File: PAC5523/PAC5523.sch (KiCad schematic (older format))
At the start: 122 parts, among them J1 CON_HALL, J2 U, J3 V, J4 W, J5 UART, J6 SWD, J7 CAN, J8 NTC, Q1 Q_NMOS_GDS, T1 Transformer_1P_1S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

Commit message: updated connectors
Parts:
- removed J1: CON_HALL, Connector_Molex:Molex_PicoBlade_53261-0571_1x05-1MP_P1.25mm_Horizontal, symbol Connector:Conn_01x06_Male
- removed J5: UART, Connector_Molex:Molex_PicoBlade_53261-0471_1x04-1MP_P1.25mm_Horizontal, symbol Connector:Conn_01x05_Male
- removed J7: CAN, Connector_Molex:Molex_PicoBlade_53261-0371_1x03-1MP_P1.25mm_Horizontal, symbol Connector:Conn_01x04_Male
- removed J8: NTC, Connector_Molex:Molex_PicoBlade_53261-0271_1x02-1MP_P1.25mm_Horizontal, symbol Connector:Conn_01x03_Male
- removed J?: LED, Connector_Molex:Molex_PicoBlade_53261-0371_1x03-1MP_P1.25mm_Horizontal, symbol Connector:Conn_01x04_Male
- added J1: UART, Connector_Molex:Molex_PicoBlade_53261-0471_1x04-1MP_P1.25mm_Horizontal, symbol Connector_Generic_MountingPin:Conn_01x04_MountingPin
- added J5: HALL, Connector_Molex:Molex_PicoBlade_53261-0571_1x05-1MP_P1.25mm_Horizontal, symbol Connector_Generic_MountingPin:Conn_01x05_MountingPin
- added J7: CAN, Connector_Molex:Molex_PicoBlade_53261-0371_1x03-1MP_P1.25mm_Horizontal, symbol Connector_Generic_MountingPin:Conn_01x03_MountingPin
- added J8: NTC, Connector_Molex:Molex_PicoBlade_53261-0271_1x02-1MP_P1.25mm_Horizontal, symbol Connector_Generic_MountingPin:Conn_01x02_MountingPin
- added J9: LED, Connector_Molex:Molex_PicoBlade_53261-0371_1x03-1MP_P1.25mm_Horizontal, symbol Connector_Generic_MountingPin:Conn_01x03_MountingPin
- gave numbers to parts that had none: 1
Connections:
- wire segments 190 -> 187
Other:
- moved on the sheet: R40
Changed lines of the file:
@@
 Text GLabel 2200 3800 3    50   Input ~ 0
 SK6812
-$Comp
-L Connector:Conn_01x04_Male J?
-U 1 1 5D45B5D1
-P 9200 9050
-F 0 "J?" H 9172 8932 50  0000 R CNN
-F 1 "LED" H 9172 9023 50  0000 R CNN
-F 2 "Connector_Molex:Molex_PicoBlade_53261-0371_1x03-1MP_P1.25mm_Horizontal" H 9200 9050 50  0001 C CNN
-F 3 "~" H 9200 9050 50  0001 C CNN
-	1    9200 9050
-	-1   0    0    1
-$EndComp
 Text GLabel 9000 9050 0    50   Input ~ 0
 SK6812_OUT
 $Comp
-L power:+5V #PWR?
+L power:+5V #PWR0133
 U 1 1 5D435A7B
 P 9000 8950
-F 0 "#PWR?" H 9000 8800 50  0001 C CNN
+F 0 "#PWR0133" H 9000 8800 50  0001 C CNN
 F 1 "+5V" V 9015 9078 50  0000 L CNN
 F 2 "" H 9000 8950 50  0001 C CNN
@@
 $EndComp
 $Comp
-L power:GND #PWR?
-U 1 1 5D42858B
-P 9000 8850
-F 0 "#PWR?" H 9000 8600 50  0001 C CNN
-F 1 "GND" V 9005 8722 50  0000 R CNN
-F 2 "" H 9000 8850 50  0001 C CNN
-F 3 "" H 9000 8850 50  0001 C CNN
-	1    9000 8850
-	0    1    1    0
-$EndComp
-$Comp
-L power:GND #PWR?
+L power:GND #PWR0157
 U 1 1 5D427763
 P 9000 9150
-F 0 "#PWR?" H 9000 8900 50  0001 C CNN
+F 0 "#PWR0157" H 9000 8900 50  0001 C CNN
 F 1 "GND" V 9005 9022 50  0000 R CNN
 F 2 "" H 9000 9150 50  0001 C CNN
@@
 	0    1    1    0
 $EndComp
-Connection ~ 8050 8950
-$Comp
-L power:GND #PWR0133
-U 1 1 5D0669EC
-P 8050 8950
-F 0 "#PWR0133" H 8050 8700 50  0001 C CNN
-F 1 "GND" H 8055 8777 50  0000 C CNN
-F 2 "" H 8050 8950 50  0001 C CNN
-F 3 "" H 8050 8950 50  0001 C CNN
-	1    8050 8950
-	-1   0    0    1
-$EndComp
-Wire Wire Line
-	8050 8950 8100 8950
-Wire Wire Line
-	8050 9050 8050 8950
-Wire Wire Line
-	8100 9050 8050 9050
 $Comp
 L Device:R_Small R40
 U 1 1 5D02818F
-P 8000 9150
-F 0 "R40" V 7804 9150 50  0000 C CNN
-F 1 "100" V 7895 9150 50  0000 C CNN
-F 2 "Resistor_SMD:R_0603_1608Metric" H 8000 9150 50  0001 C CNN
-F 3 "~" H 8000 9150 50  0001 C CNN
-	1    8000 9150
+P 7800 9150
+F 0 "R40" V 7604 9150 50  0000 C CNN
+F 1 "100" V 7695 9150 50  0000 C CNN
+F 2 "Resistor_SMD:R_0603_1608Metric" H 7800 9150 50  0001 C CNN
+F 3 "~" H 7800 9150 50  0001 C CNN
+	1    7800 9150
 	0    -1   -1   0
 $EndComp
-Text GLabel 7900 9150 0    50   Input ~ 0
+Text GLabel 7700 9150 0    50   Input ~ 0
 NTC
-$Comp
-L Connector:Conn_01x03_Male J8
-U 1 1 5D010531
-P 8300 9050
-F 0 "J8" H 8408 9331 50  0000 C CNN
-F 1 "NTC" H 8408 9240 50  0000 C CNN
-F 2 "Connector_Molex:Molex_PicoBlade_53261-0271_1x02-1MP_P1.25mm_Horizontal" H 8300 9050 50  0001 C CNN
-F 3 "~" H 8300 9050 50  0001 C CNN
-	1    8300 9050
-	-1   0    0    1
-$EndComp
 $Comp
 L power:GND #PWR0146
 U 1 1 5D12B3D5
-P 6850 8850
-F 0 "#PWR0146" H 6850 8600 50  0001 C CNN
-F 1 "GND" H 6855 8677 50  0000 C CNN
-F 2 "" H 6850 8850 50  0001 C CNN
-F 3 "" H 6850 8850 50  0001 C CNN
-	1    6850 8850
-	0    1    1    0
-$EndComp
-$Comp
-L Connector:Conn_01x04_Male J7
-U 1 1 5D12AA35
-P 7050 9050
-F 0 "J7" H 7022 8932 50  0000 R CNN
-F 1 "CAN" H 7022 9023 50  0000 R CNN
-F 2 "Connector_Molex:Molex_PicoBlade_53261-0371_1x03-1MP_P1.25mm_Horizontal" H 7050 9050 50  0001 C CNN
-F 3 "~" H 7050 9050 50  0001 C CNN
-	1    7050 9050
-	-1   0    0    1
+P 7050 9350
+F 0 "#PWR0146" H 7050 9100 50  0001 C CNN
+F 1 "GND" H 7055 9177 50  0000 C CNN
+F 2 "" H 7050 9350 50  0001 C CNN
+F 3 "" H 7050 9350 50  0001 C CNN
+	1    7050 9350
+	1    0    0    -1
 $EndComp
 Text GLabel 6850 8950 0    50   Input ~ 0
@@
 $EndComp
 $Comp
-L power:+5V #PWR?
+L power:+5V #PWR0158
 U 1 1 5D3E7529
 P 5700 8550
-F 0 "#PWR?" H 5700 8400 50  0001 C CNN
+F 0 "#PWR0158" H 5700 8400 50  0001 C CNN
 F 1 "+5V" V 5715 8678 50  0000 L CNN
 F 2 "" H 5700 8550 50  0001 C CNN
@@
 	0    1    1    0
 $EndComp
-Connection ~ 5450 9300
 Wire Wire Line
 	5450 9300 5450 9200
@@
 $EndComp
 $Comp
-L Connector:Conn_01x06_Male J1
-U 1 1 5CD1FDBA
-P 5650 9100
-F 0 "J1" H 5622 8982 50  0000 R CNN
-F 1 "CON_HALL" H 5622 9073 50  0000 R CNN
-F 2 "Connector_Molex:Molex_PicoBlade_53261-0571_1x05-1MP_P1.25mm_Horizontal" H 5650 9100 50  0001 C CNN
-F 3 "~" H 5650 9100 50  0001 C CNN
-	1    5650 9100
-	-1   0    0    1
-$EndComp
-$Comp
 L Device:R_Small R5
 U 1 1 5CCEC271
@@
 	1900 9000 1900 9400
 $Comp
-L power:+5V #PWR?
+L power:+5V #PWR0159
 U 1 1 5D3F5601
 P 1650 9550
-F 0 "#PWR?" H 1650 9400 50  0001 C CNN
+F 0 "#PWR0159" H 1650 9400 50  0001 C CNN
 F 1 "+5V" V 1665 9678 50  0000 L CNN
 F 2 "" H 1650 9550 50  0001 C CNN
@@
 $EndComp
 $Comp
-L Jumper:Jumper_3_Bridged12 JP?
+L Jumper:Jumper_3_Bridged12 JP4
 U 1 1 5D3F55FB
 P 1900 9550
-F 0 "JP?" H 1900 9754 50  0000 C CNN
+F 0 "JP4" H 1900 9754 50  0000 C CNN
 F 1 "HALL_V" H 1900 9663 50  0000 C CNN
 F 2 "Jumper:SolderJumper-3_P1.3mm_Bridged2Bar12_Pad1.0x1.5mm" H 1900 9550 50  0001 C CNN
@@
 Wire Wire Line
 	2150 9100 2400 9100
-$Comp
-L Connector:Conn_01x05_Male J5
-U 1 1 5D34B76B
-P 2600 9100
-F 0 "J5" H 2572 9032 50  0000 R CNN
-F 1 "UART" H 2572 9123 50  0000 R CNN
-F 2 "Connector_Molex:Molex_PicoBlade_53261-0471_1x04-1MP_P1.25mm_Horizontal" H 2600 9100 50  0001 C CNN
-F 3 "~" H 2600 9100 50  0001 C CNN
-	1    2600 9100
-	-1   0    0    1
-$EndComp
 Text GLabel 1800 8450 0    50   Input ~ 0
 RS485_A
@@
 SWDIO
 $Comp
-L power:+5V #PWR?
+L power:+5V #PWR0160
 U 1 1 5D442696
 P -850 350
-F 0 "#PWR?" H -850 200 50  0001 C CNN
+F 0 "#PWR0160" H -850 200 50  0001 C CNN
 F 1 "+5V" V -835 478 50  0000 L CNN
 F 2 "" H -850 350 50  0001 C CNN
@@
 Connection ~ -200 -950
 $Comp
-L power:+5V #PWR?
+L power:+5V #PWR0161
 U 1 1 5D3E57C8
 P -200 -950
-F 0 "#PWR?" H -200 -1100 50  0001 C CNN
+F 0 "#PWR0161" H -200 -1100 50  0001 C CNN
 F 1 "+5V" H -185 -777 50  0000 C CNN
 F 2 "" H -200 -950 50  0001 C CNN
@@
 	1    0    0    -1
 $EndComp
+$Comp
+L Connector_Generic_MountingPin:Conn_01x03_MountingPin J7
+U 1 1 5D51AF1E
+P 7050 9050
+F 0 "J7" H 7138 9014 50  0000 L CNN
+F 1 "CAN" H 7138 8923 50  0000 L CNN
+F 2 "Connector_Molex:Molex_PicoBlade_53261-0371_1x03-1MP_P1.25mm_Horizontal" H 7050 9050 50  0001 C CNN
+F 3 "~" H 7050 9050 50  0001 C CNN
+	1    7050 9050
+	1    0    0    -1
+$EndComp
+$Comp
+L power:GND #PWR0162
+U 1 1 5D51CD51
+P 9200 9350
+F 0 "#PWR0162" H 9200 9100 50  0001 C CNN
+F 1 "GND" H 9205 9177 50  0000 C CNN
+F 2 "" H 9200 9350 50  0001 C CNN
+F 3 "" H 9200 9350 50  0001 C CNN
+	1    9200 9350
+	1    0    0    -1
+$EndComp
+$Comp
+L Connector_Generic_MountingPin:Conn_01x03_MountingPin J9
+U 1 1 5D51CD57
+P 9200 9050
+F 0 "J9" H 9288 9014 50  0000 L CNN
+F 1 "LED" H 9288 8923 50  0000 L CNN
+F 2 "Connector_Molex:Molex_PicoBlade_53261-0371_1x03-1MP_P1.25mm_Horizontal" H 9200 9050 50  0001 C CNN
+F 3 "~" H 9200 9050 50  0001 C CNN
+	1    9200 9050
+	1    0    0    -1
+$EndComp
+$Comp
+L Connector_Generic_MountingPin:Conn_01x02_MountingPin J8
+U 1 1 5D536607
+P 8100 9050
+F 0 "J8" H 8188 8964 50  0000 L CNN
+F 1 "NTC" H 8188 8873 50  0000 L CNN
+F 2 "Connector_Molex:Molex_PicoBlade_53261-0271_1x02-1MP_P1.25mm_Horizontal" H 8100 9050 50  0001 C CNN
+F 3 "~" H 8100 9050 50  0001 C CNN
+	1    8100 9050
+	1    0    0    -1
+$EndComp
+$Comp
+L power:GND #PWR0163
+U 1 1 5D536E3F
+P 8100 9350
+F 0 "#PWR0163" H 8100 9100 50  0001 C CNN
+F 1 "GND" H 8105 9177 50  0000 C CNN
+F 2 "" H 8100 9350 50  0001 C CNN
+F 3 "" H 8100 9350 50  0001 C CNN
+	1    8100 9350
+	1    0    0    -1
+$EndComp
+$Comp
+L power:GND #PWR0164
+U 1 1 5D542586
+P 7900 9050
+F 0 "#PWR0164" H 7900 8800 50  0001 C CNN
+F 1 "GND" H 7905 8877 50  0000 C CNN
+F 2 "" H 7900 9050 50  0001 C CNN
+F 3 "" H 7900 9050 50  0001 C CNN
+	1    7900 9050
+	0    1    1    0
+$EndComp
+$Comp
+L Connector_Generic_MountingPin:Conn_01x05_MountingPin J5
+U 1 1 5D54F00B
+P 5650 9000
+F 0 "J5" H 5738 8964 50  0000 L CNN
+F 1 "HALL" H 5738 8873 50  0000 L CNN
+F 2 "Connector_Molex:Molex_PicoBlade_53261-0571_1x05-1MP_P1.25mm_Horizontal" H 5650 9000 50  0001 C CNN
+F 3 "~" H 5650 9000 50  0001 C CNN
+	1    5650 9000
+	1    0    0    -1
+$EndComp
+$Comp
+L power:GND #PWR0165
+U 1 1 5D550080
+P 5650 9400
+F 0 "#PWR0165" H 5650 9150 50  0001 C CNN
+F 1 "GND" H 5655 9227 50  0000 C CNN
+F 2 "" H 5650 9400 50  0001 C CNN
+F 3 "" H 5650 9400 50  0001 C CNN
+	1    5650 9400
+	1    0    0    -1
+$EndComp
+$Comp
+L Connector_Generic_MountingPin:Conn_01x04_MountingPin J1
+U 1 1 5D55190A
+P 2600 9100
+F 0 "J1" H 2688 9014 50  0000 L CNN
+F 1 "UART" H 2688 8923 50  0000 L CNN
+F 2 "Connector_Molex:Molex_PicoBlade_53261-0471_1x04-1MP_P1.25mm_Horizontal" H 2600 9100 50  0001 C CNN
+F 3 "~" H 2600 9100 50  0001 C CNN
+	1    2600 9100
+	1    0    0    -1
+$EndComp
+$Comp
+L power:GND #PWR0166
+U 1 1 5D551E10
+P 2600 9500
+F 0 "#PWR0166" H 2600 9250 50  0001 C CNN
+F 1 "GND" V 2605 9372 50  0000 R CNN
+F 2 "" H 2600 9500 50  0001 C CNN
+F 3 "" H 2600 9500 50  0001 C CNN
+	1    2600 9500
+	1    0    0    -1
+$EndComp

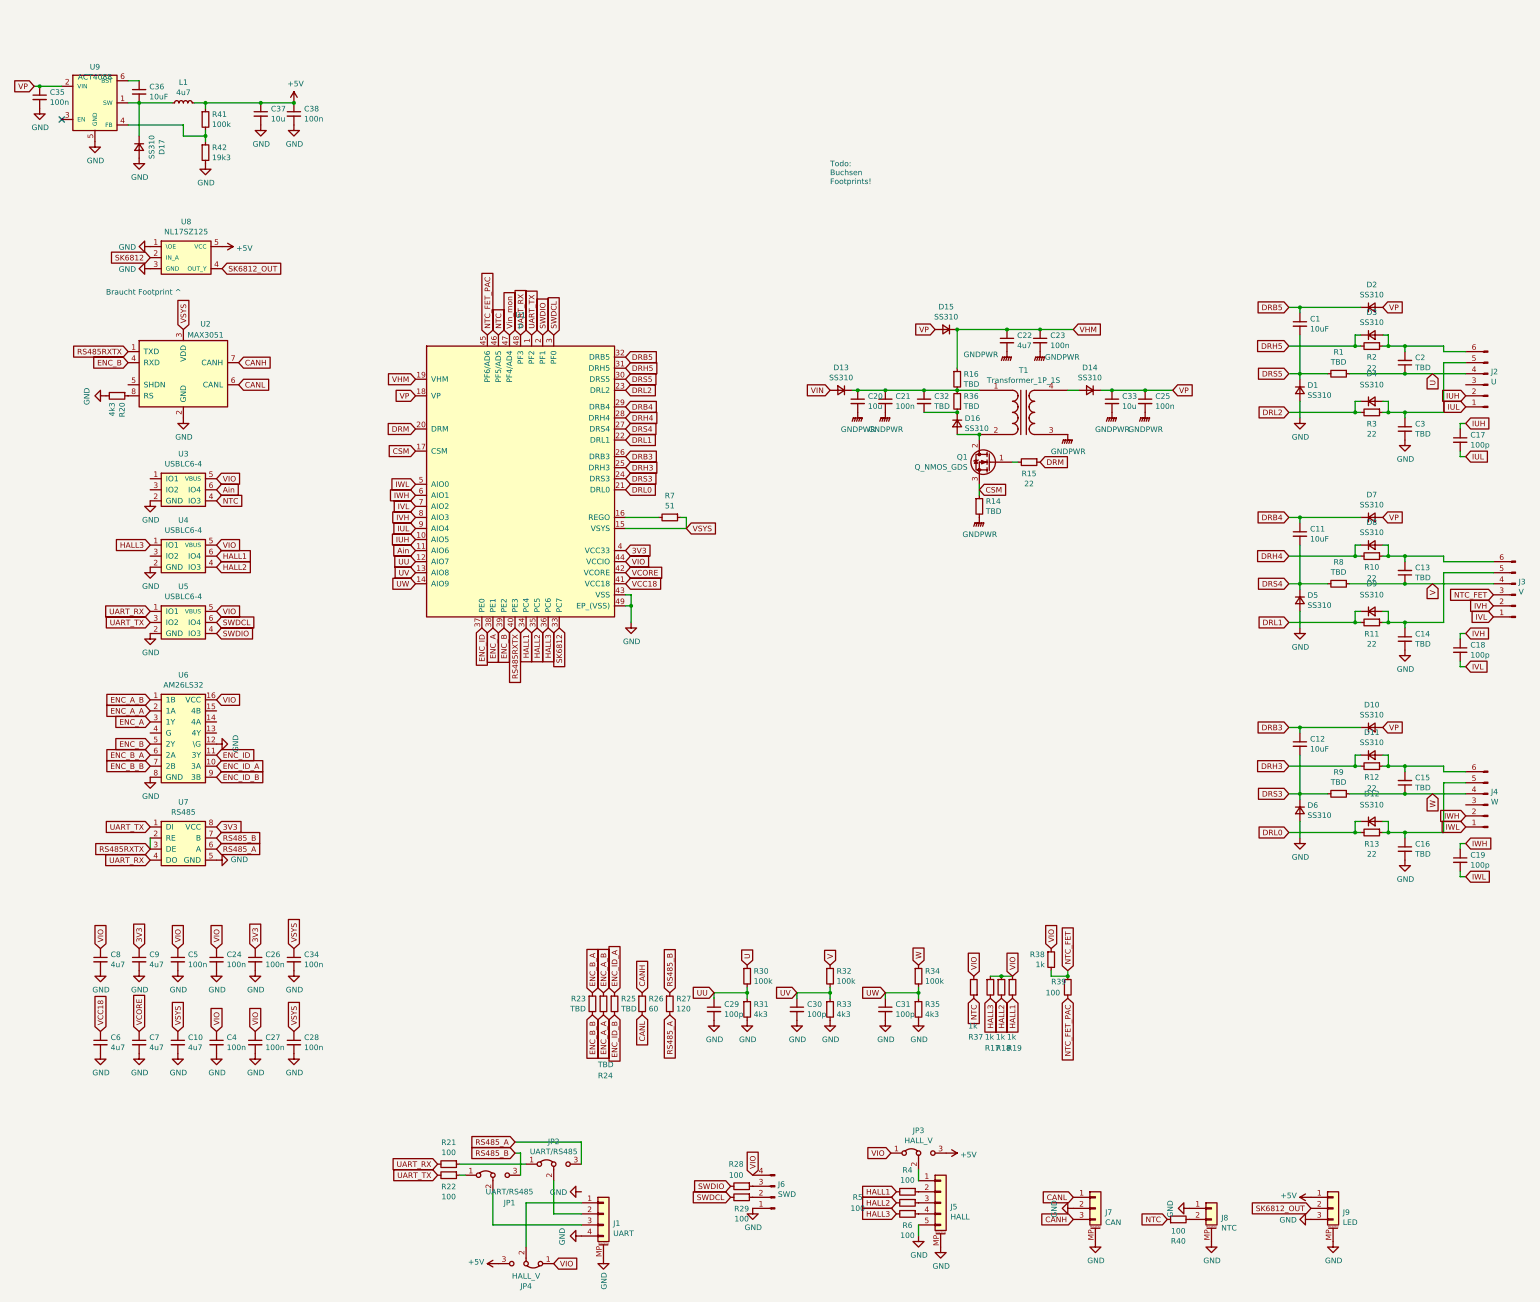
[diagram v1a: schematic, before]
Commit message: schematic cleanup, added PDF
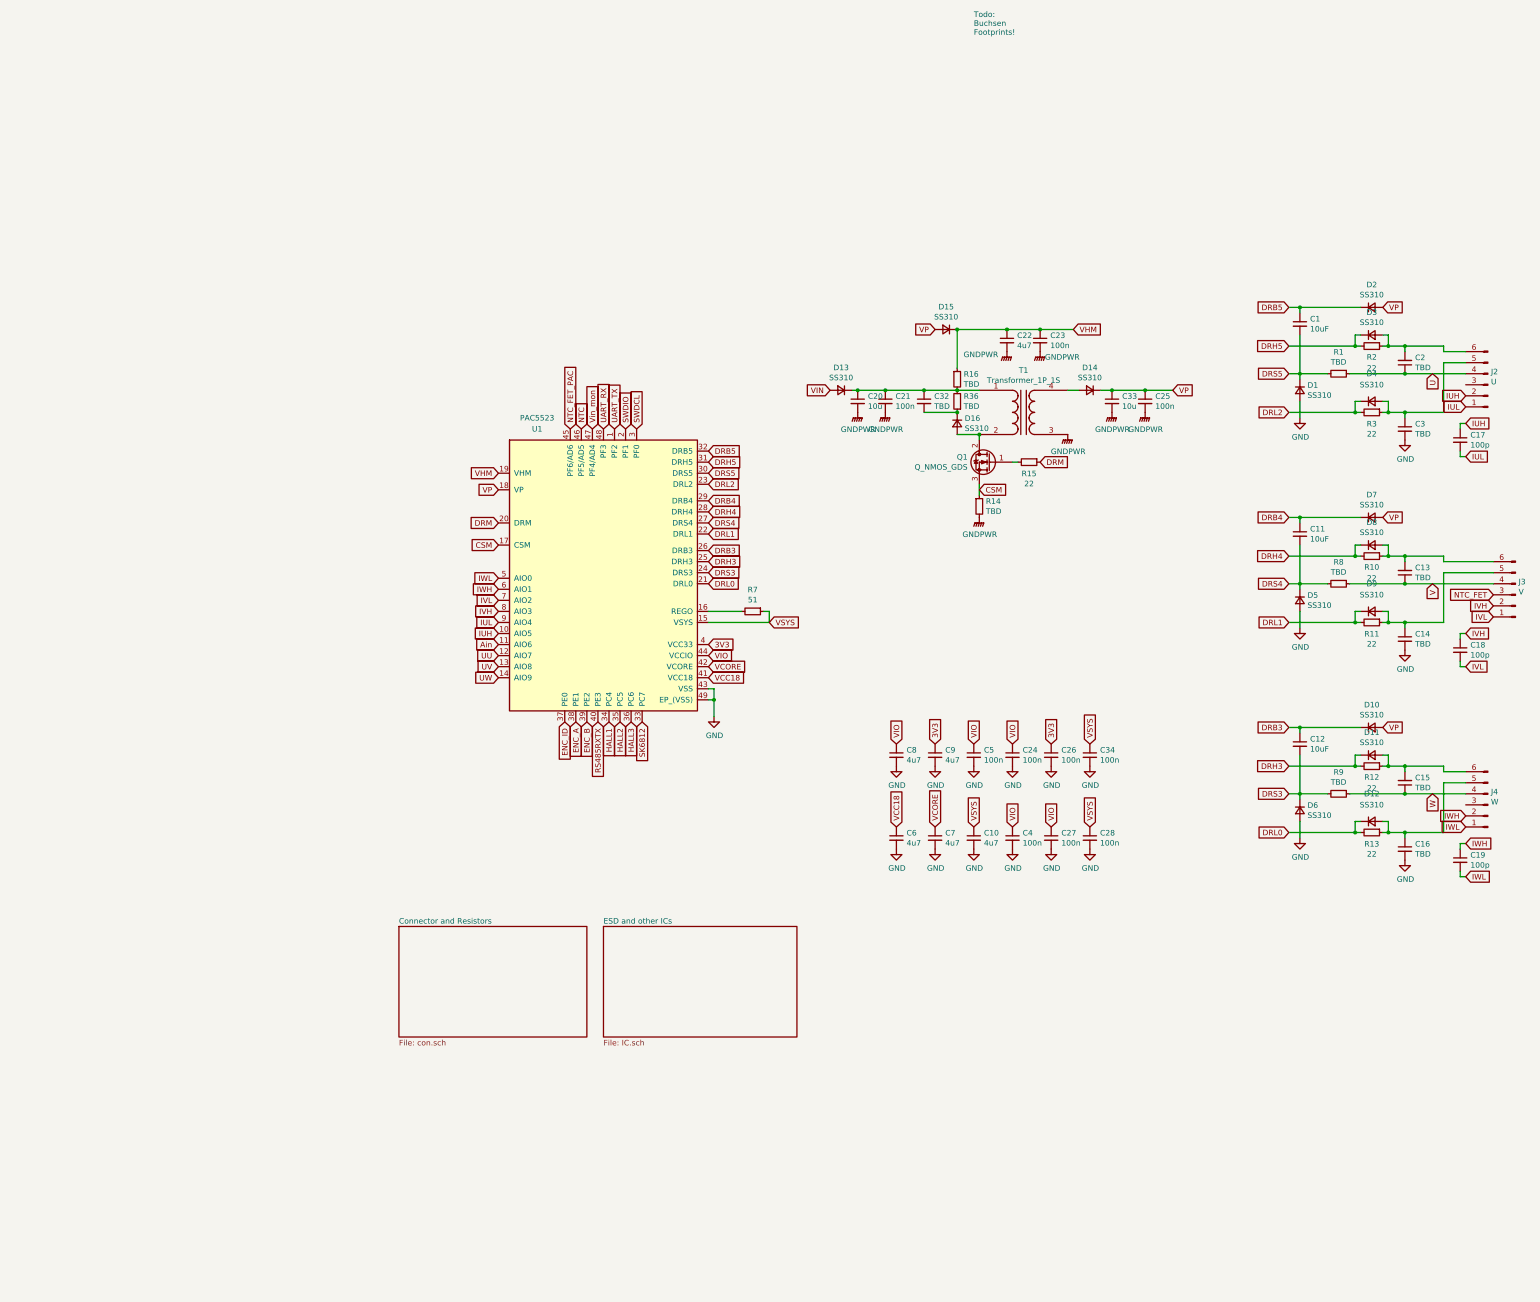
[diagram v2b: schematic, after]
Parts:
- removed C29, C30, C31: 100p, Capacitor_SMD:C_0603_1608Metric, symbol Device:C_Small
- removed C35, C38: 100n, Capacitor_SMD:C_0603_1608Metric, symbol Device:C_Small
- removed C36: 10uF, Capacitor_SMD:C_0805_2012Metric, symbol Device:C_Small
- removed C37: 10u, Capacitor_SMD:C_1206_3216Metric, symbol Device:C_Small
- removed D17: SS310, Diode_SMD:D_SMA, symbol Device:D_Small
- removed J1: UART, Connector_Molex:Molex_PicoBlade_53261-0471_1x04-1MP_P1.25mm_Horizontal, symbol Connector_Generic_MountingPin:Conn_01x04_MountingPin
- removed J5: HALL, Connector_Molex:Molex_PicoBlade_53261-0571_1x05-1MP_P1.25mm_Horizontal, symbol Connector_Generic_MountingPin:Conn_01x05_MountingPin
- removed J6: SWD, Connector_PinHeader_2.54mm:PinHeader_1x04_P2.54mm_Vertical, symbol Connector:Conn_01x04_Male
- removed J7: CAN, Connector_Molex:Molex_PicoBlade_53261-0371_1x03-1MP_P1.25mm_Horizontal, symbol Connector_Generic_MountingPin:Conn_01x03_MountingPin
- removed J8: NTC, Connector_Molex:Molex_PicoBlade_53261-0271_1x02-1MP_P1.25mm_Horizontal, symbol Connector_Generic_MountingPin:Conn_01x02_MountingPin
- removed J9: LED, Connector_Molex:Molex_PicoBlade_53261-0371_1x03-1MP_P1.25mm_Horizontal, symbol Connector_Generic_MountingPin:Conn_01x03_MountingPin
- removed JP1, JP2: UART/RS485, Jumper:SolderJumper-3_P1.3mm_Bridged2Bar12_Pad1.0x1.5mm, symbol Jumper:Jumper_3_Bridged12
- removed JP3, JP4: HALL_V, Jumper:SolderJumper-3_P1.3mm_Bridged2Bar12_Pad1.0x1.5mm, symbol Jumper:Jumper_3_Bridged12
- removed L1: 4u7, Inductor_SMD:L_Taiyo-Yuden_MD-4040, symbol Device:L_Small
- removed R17, R18, R19, R37, R38: 1k, Resistor_SMD:R_0603_1608Metric, symbol Device:R_Small
- removed R20, R31, R33, R35: 4k3, Resistor_SMD:R_0603_1608Metric, symbol Device:R_Small
- removed R21, R22, R28, R29, R39, R4, R40, R5, R6: 100, Resistor_SMD:R_0603_1608Metric, symbol Device:R_Small
- removed R23, R24, R25: TBD, Resistor_SMD:R_0603_1608Metric, symbol Device:R_Small
- removed R26: 60, Resistor_SMD:R_0603_1608Metric, symbol Device:R_Small
- removed R27: 120, Resistor_SMD:R_0603_1608Metric, symbol Device:R_Small
- removed R30, R32, R34, R41: 100k, Resistor_SMD:R_0603_1608Metric, symbol Device:R_Small
- removed R42: 19k3, Resistor_SMD:R_0603_1608Metric, symbol Device:R_Small
- removed U2: MAX3051, Package_SO:SOIC-8_3.9x4.9mm_P1.27mm, symbol Interface_UART:MAX3051
- removed U3, U4, U5: USBLC6-4, Package_TO_SOT_SMD:SOT-23-6, symbol otter:USBLC6-4
- removed U6: AM26LS32, Package_SO:SOIC-16W_5.3x10.2mm_P1.27mm, symbol otter:AM26LS32
- removed U7: RS485, Package_SO:SOIC-8_3.9x4.9mm_P1.27mm, symbol otter:RS485
- removed U8: NL17SZ125, symbol otter:NL17SZ125
- removed U9: ACT4088, Package_TO_SOT_SMD:SOT-23-6, symbol otter:ACT4088
- U1: value p -> PAC5523
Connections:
- no-connect marks 1 -> 0
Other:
- note removed: "Braucht Footprint ^"
- moved on the sheet: C10, C24, C26, C27, C28, C34, C4, C5, C6, C7, C8, C9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

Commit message: updated schematic
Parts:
- C1, C11, C12: value 10uF -> 1uF
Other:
- note added: "TVS Diode\nWiderstand"
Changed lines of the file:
@@
 P 8900 1050
 F 0 "C1" H 8992 1096 50  0000 L CNN
-F 1 "10uF" H 8992 1005 50  0000 L CNN
+F 1 "1uF" H 8992 1005 50  0000 L CNN
 F 2 "Capacitor_SMD:C_0805_2012Metric" H 8900 1050 50  0001 C CNN
 F 3 "~" H 8900 1050 50  0001 C CNN
@@
 P 8900 2950
 F 0 "C11" H 8992 2996 50  0000 L CNN
-F 1 "10uF" H 8992 2905 50  0000 L CNN
+F 1 "1uF" H 8992 2905 50  0000 L CNN
 F 2 "Capacitor_SMD:C_0805_2012Metric" H 8900 2950 50  0001 C CNN
 F 3 "~" H 8900 2950 50  0001 C CNN
@@
 P 8900 4850
 F 0 "C12" H 8992 4896 50  0000 L CNN
-F 1 "10uF" H 8992 4805 50  0000 L CNN
+F 1 "1uF" H 8992 4805 50  0000 L CNN
 F 2 "Capacitor_SMD:C_0805_2012Metric" H 8900 4850 50  0001 C CNN
 F 3 "~" H 8900 4850 50  0001 C CNN
@@
 F1 "IC.sch" 50
 $EndSheet
+Text Notes 5100 1550 0    50   ~ 0
+TVS Diode\nWiderstand
 $EndSCHEMATC
